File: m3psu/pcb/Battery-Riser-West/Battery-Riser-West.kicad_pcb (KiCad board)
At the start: 2 copper layers, 20 x 67.5 mm, 2 parts, among them J1 WEST TOP, J2 WEST BOT

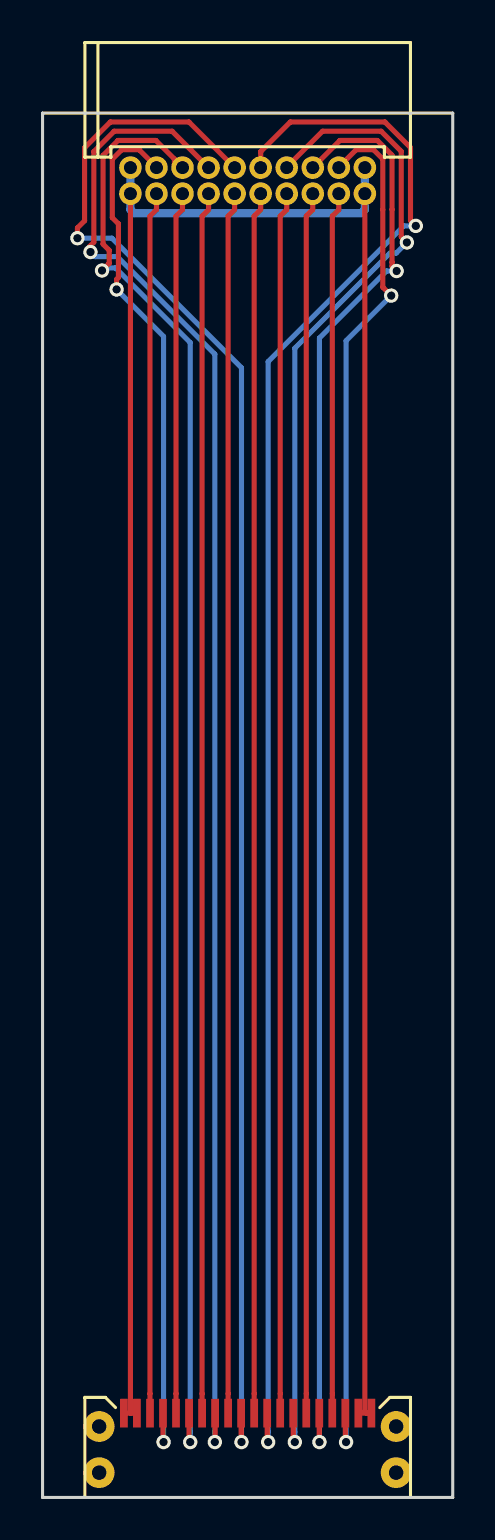
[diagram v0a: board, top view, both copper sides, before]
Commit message: Fix trace widths and spacing on riser boards
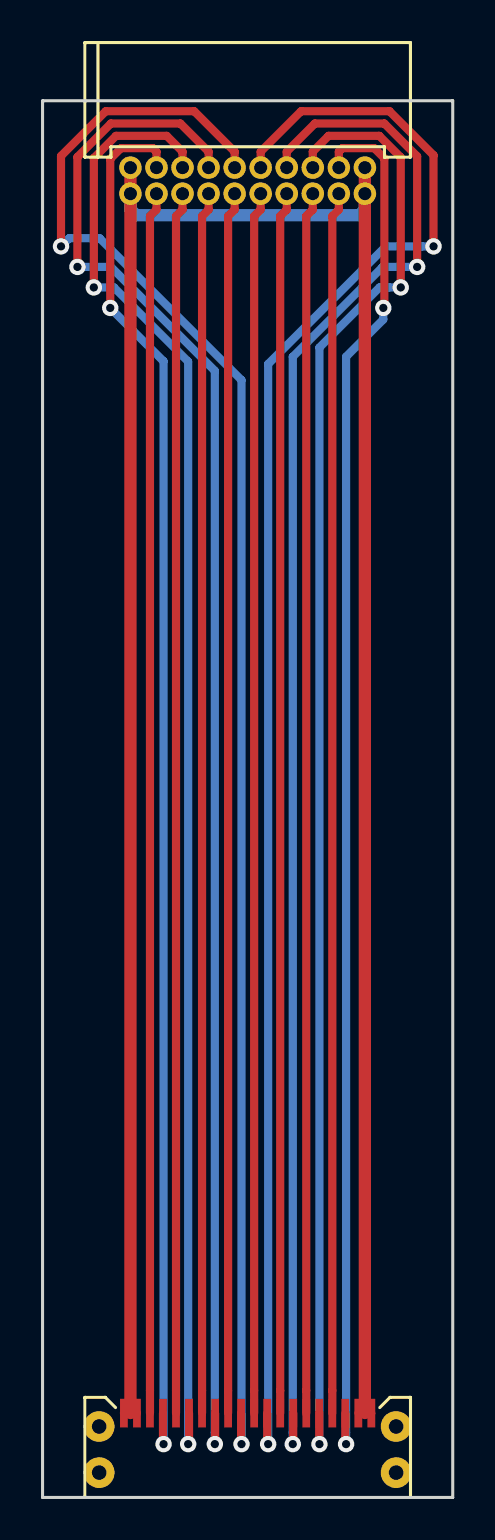
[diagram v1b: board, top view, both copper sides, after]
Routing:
- net /3v3_DL: track 77.7 -> 80.6 mm
- net /3v3_PYRO: track 77.2 -> 80.0 mm
- net /3v3_FC: track 73.7 -> 76.2 mm
- net /3v3_AUX1: track 74.3 -> 76.4 mm
- net /3v3_RADIO: track 70.8 -> 72.3 mm
- net /RSVD3: track 71.7 -> 72.6 mm
- net /RSVD2: track 67.8 -> 68.6 mm
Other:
- board size 20 x 67.5 mm -> 20 x 68.1 mm

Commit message: Widen tracks, add logo, fix DRC errors in West riser.
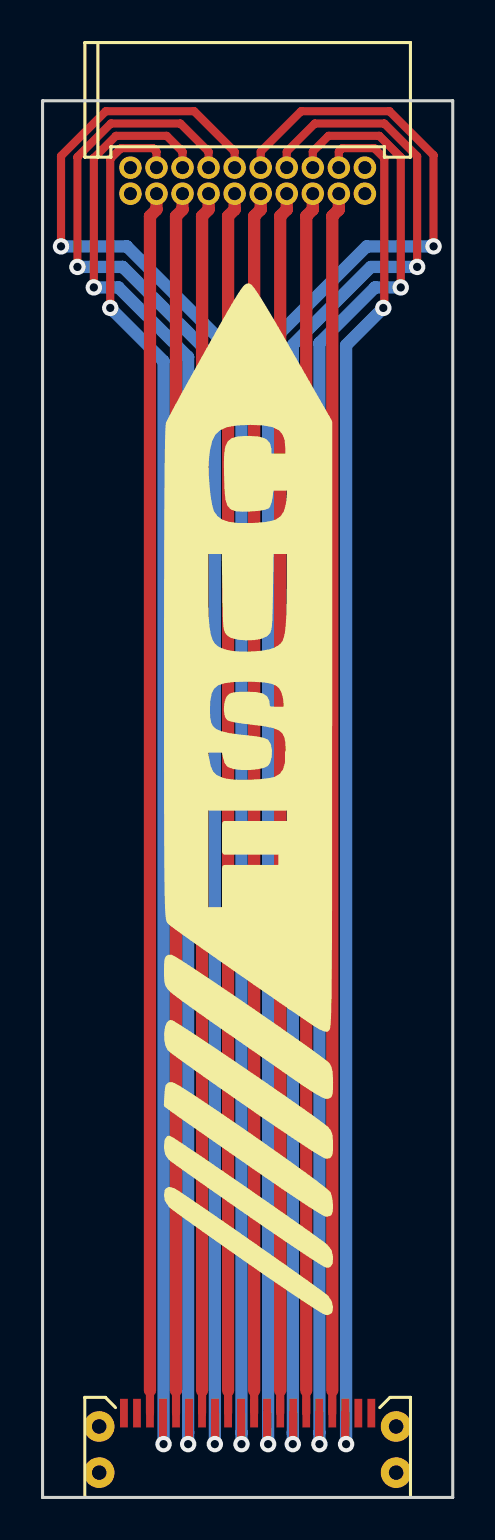
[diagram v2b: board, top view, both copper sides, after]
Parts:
- added G***: LOGO, m3psu:cusf_logo_large, F.Cu at (156.0, 96.0)
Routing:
- net GND: track 135.9 -> 0.00 mm
- net /3v3_PYRO: track 80.0 -> 80.5 mm
- added copper zone on B.Cu, net GND
- added copper zone on F.Cu, net GND
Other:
- rule pad_to_mask_clearance: 0.2 -> 0.15

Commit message: fix riser ground pour, stitching, silk, mask clearance, generate gerbers
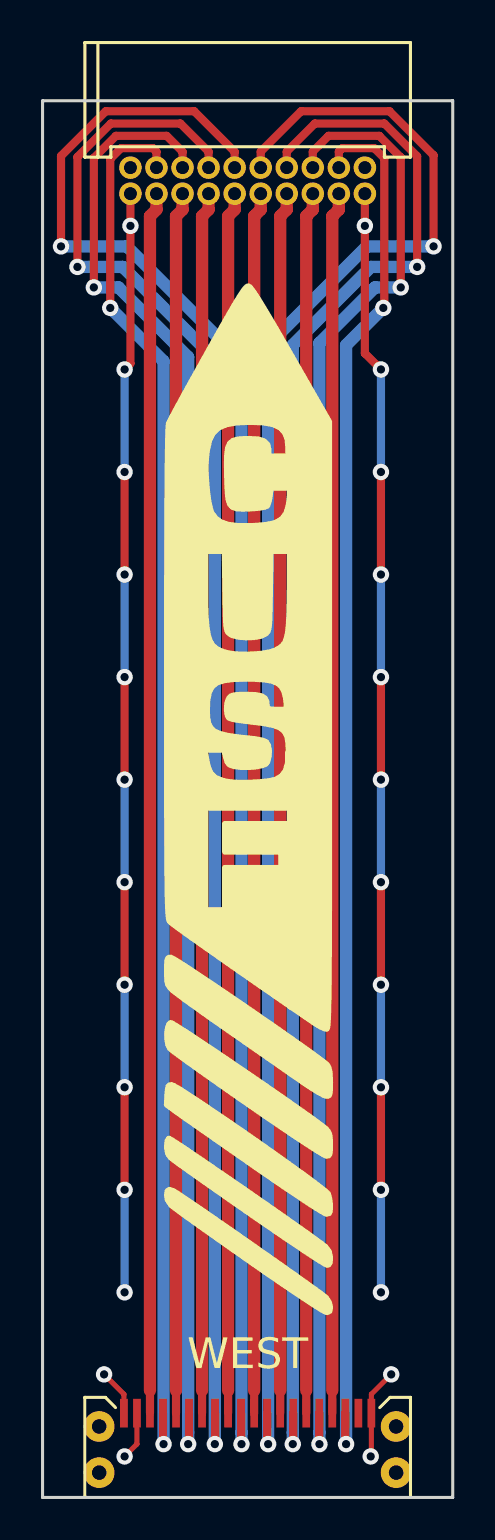
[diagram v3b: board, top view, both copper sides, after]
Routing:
- net GND: track 0.00 -> 119.8 mm, vias 0 -> 26
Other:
- rule pad_to_mask_clearance: 0.15 -> 0
- board text added: "WEST"
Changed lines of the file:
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@@
-(kicad_pcb (version 4) (host pcbnew 4.0.0-rc2-stable)
+(kicad_pcb (version 4) (host pcbnew 4.1.0-alpha+201605071002+6776~44~ubuntu14.04.1-product)
   (general
     (links 23)
     (no_connects 0)
-    (area 145.825 58.644999 166.075001 135.355001)
+    (area 145.924999 58.644999 166.075001 135.355001)
     (thickness 1.6)
-    (drawings 4)
-    (tracks 132)
+    (drawings 5)
+    (tracks 192)
     (zones 0)
     (modules 3)
@@
   (page A4)
   (layers
-    (0 F.Cu signal hide)
-    (31 B.Cu signal hide)
+    (0 F.Cu signal)
+    (31 B.Cu signal)
     (32 B.Adhes user)
     (33 F.Adhes user)
@@
     (user_trace_width 0.8)
     (trace_clearance 0.15)
-    (zone_clearance 0.2)
+    (zone_clearance 0.3)
     (zone_45_only no)
     (trace_min 0.2)
@@
     (pad_size 1.524 1.524)
     (pad_drill 0.762)
-    (pad_to_mask_clearance 0.15)
+    (pad_to_mask_clearance 0)
     (aux_axis_origin 0 0)
     (visible_elements 7FFFFFFF)
     (pcbplotparams
-      (layerselection 0x00030_80000001)
-      (usegerberextensions false)
+      (layerselection 0x010f0_ffffffff)
+      (usegerberextensions true)
       (excludeedgelayer true)
       (linewidth 0.100000)
@@
       (hpglpenspeed 20)
       (hpglpendiameter 15)
-      (hpglpenoverlay 2)
       (psnegative false)
       (psa4output false)
-      (plotreference true)
-      (plotvalue true)
+      (plotreference false)
+      (plotvalue false)
       (plotinvisibletext false)
       (padsonsilk false)
-      (subtractmaskfromsilk false)
+      (subtractmaskfromsilk true)
       (outputformat 1)
       (mirror false)
-      (drillshape 1)
+      (drillshape 0)
       (scaleselection 1)
-      (outputdirectory ""))
+      (outputdirectory gerbers/))
   )
   (net 0 "")
@@
   (module agg:SFM-110-02-L-DH (layer F.Cu)
     (at 156 129.7 180)
-    (fp_text reference J2 (at 9.1 2.6 450) (layer F.Fab)
+    (fp_text reference J2 (at 9.1 2.6 90) (layer F.Fab)
       (effects (font (size 1 1) (thickness 0.15)))
     )
@@
   (module agg:TFML-110-01-L-D-RA (layer F.Cu)
     (at 156 63 180)
-    (fp_text reference J1 (at 9 -2 450) (layer F.Fab)
+    (fp_text reference J1 (at 9 -2 90) (layer F.Fab)
       (effects (font (size 1 1) (thickness 0.15)))
     )
@@
       (xy 3.986213 -3.606549) (xy 3.986213 -3.606549)) (layer F.SilkS) (width 0.27))
   )
+  (gr_text WEST (at 156 123) (layer F.SilkS)
+    (effects (font (size 1.5 1.5) (thickness 0.3)))
+  )
   (gr_line (start 166 130) (end 146 130) (layer Edge.Cuts) (width 0.15))
   (gr_line (start 146 61.9) (end 166 61.9) (layer Edge.Cuts) (width 0.15))
   (gr_line (start 166 61.9) (end 166 130) (layer Edge.Cuts) (width 0.15))
   (gr_line (start 146 130) (end 146 61.9) (layer Edge.Cuts) (width 0.15))
+  (segment (start 161.715 66.429) (end 161.715 68) (width 0.4) (layer F.Cu) (net 1))
+  (segment (start 161.715 68) (end 161.715 74.215) (width 0.4) (layer F.Cu) (net 1))
+  (segment (start 161.715 66.429) (end 161.715 68) (width 0.25) (layer B.Cu) (net 1))
+  (via (at 161.715 68) (size 0.8) (drill 0.4) (layers F.Cu B.Cu) (net 1))
+  (segment (start 150.285 66.429) (end 150.285 68) (width 0.4) (layer F.Cu) (net 1))
+  (segment (start 150.285 68) (end 150.285 74.715) (width 0.4) (layer F.Cu) (net 1))
+  (segment (start 150.285 66.429) (end 150.285 68) (width 0.25) (layer B.Cu) (net 1))
+  (via (at 150.285 68) (size 0.8) (drill 0.4) (layers F.Cu B.Cu) (net 1))
+  (segment (start 162.0325 125.89) (end 162.0325 124.9675) (width 0.25) (layer F.Cu) (net 1))
+  (segment (start 162.0325 124.9675) (end 163 124) (width 0.25) (layer F.Cu) (net 1))
+  (via (at 163 124) (size 0.8) (drill 0.4) (layers F.Cu B.Cu) (net 1))
+  (segment (start 162.0325 125.89) (end 162.0325 127.9675) (width 0.25) (layer F.Cu) (net 1))
+  (segment (start 162.0325 127.9675) (end 162 128) (width 0.25) (layer F.Cu) (net 1))
+  (via (at 162 128) (size 0.8) (drill 0.4) (layers F.Cu B.Cu) (net 1))
+  (segment (start 150.6025 125.89) (end 150.6025 127.3975) (width 0.25) (layer F.Cu) (net 1))
+  (segment (start 150.6025 127.3975) (end 150 128) (width 0.25) (layer F.Cu) (net 1))
+  (via (at 150 128) (size 0.8) (drill 0.4) (layers F.Cu B.Cu) (net 1))
+  (segment (start 149.9675 125.89) (end 149.9675 124.9675) (width 0.25) (layer F.Cu) (net 1))
+  (segment (start 149.9675 124.9675) (end 149 124) (width 0.25) (layer F.Cu) (net 1))
+  (via (at 149 124) (size 0.8) (drill 0.4) (layers F.Cu B.Cu) (net 1))
+  (segment (start 162.5 115) (end 162.5 120) (width 0.4) (layer B.Cu) (net 1))
+  (via (at 162.5 120) (size 0.8) (drill 0.4) (layers F.Cu B.Cu) (net 1))
+  (segment (start 162.5 110) (end 162.5 115) (width 0.4) (layer F.Cu) (net 1))
+  (via (at 162.5 115) (size 0.8) (drill 0.4) (layers F.Cu B.Cu) (net 1))
+  (segment (start 162.5 105) (end 162.5 110) (width 0.4) (layer B.Cu) (net 1))
+  (via (at 162.5 110) (size 0.8) (drill 0.4) (layers F.Cu B.Cu) (net 1))
+  (segment (start 162.5 100) (end 162.5 105) (width 0.4) (layer F.Cu) (net 1))
+  (via (at 162.5 105) (size 0.8) (drill 0.4) (layers F.Cu B.Cu) (net 1))
+  (segment (start 162.5 95) (end 162.5 100) (width 0.4) (layer B.Cu) (net 1))
+  (via (at 162.5 100) (size 0.8) (drill 0.4) (layers F.Cu B.Cu) (net 1))
+  (segment (start 162.5 90) (end 162.5 95) (width 0.4) (layer F.Cu) (net 1))
+  (via (at 162.5 95) (size 0.8) (drill 0.4) (layers F.Cu B.Cu) (net 1))
+  (segment (start 162.5 85) (end 162.5 90) (width 0.4) (layer B.Cu) (net 1))
+  (via (at 162.5 90) (size 0.8) (drill 0.4) (layers F.Cu B.Cu) (net 1))
+  (segment (start 162.5 80) (end 162.5 85) (width 0.4) (layer F.Cu) (net 1))
+  (via (at 162.5 85) (size 0.8) (drill 0.4) (layers F.Cu B.Cu) (net 1))
+  (segment (start 162.5 75) (end 162.5 80) (width 0.4) (layer B.Cu) (net 1))
+  (via (at 162.5 80) (size 0.8) (drill 0.4) (layers F.Cu B.Cu) (net 1))
+  (segment (start 161.715 74.215) (end 162.5 75) (width 0.4) (layer F.Cu) (net 1))
+  (via (at 162.5 75) (size 0.8) (drill 0.4) (layers F.Cu B.Cu) (net 1))
+  (segment (start 150 115) (end 150 120) (width 0.4) (layer B.Cu) (net 1))
+  (via (at 150 120) (size 0.8) (drill 0.4) (layers F.Cu B.Cu) (net 1))
+  (segment (start 150 110) (end 150 115) (width 0.4) (layer F.Cu) (net 1))
+  (via (at 150 115) (size 0.8) (drill 0.4) (layers F.Cu B.Cu) (net 1))
+  (segment (start 150 105) (end 150 110) (width 0.4) (layer B.Cu) (net 1))
+  (via (at 150 110) (size 0.8) (drill 0.4) (layers F.Cu B.Cu) (net 1))
+  (segment (start 150 100) (end 150 105) (width 0.4) (layer F.Cu) (net 1))
+  (via (at 150 105) (size 0.8) (drill 0.4) (layers F.Cu B.Cu) (net 1))
+  (segment (start 150 95) (end 150 100) (width 0.4) (layer B.Cu) (net 1))
+  (via (at 150 100) (size 0.8) (drill 0.4) (layers F.Cu B.Cu) (net 1))
+  (segment (start 150 90) (end 150 95) (width 0.4) (layer F.Cu) (net 1))
+  (via (at 150 95) (size 0.8) (drill 0.4) (layers F.Cu B.Cu) (net 1))
+  (segment (start 150 85) (end 150 90) (width 0.4) (layer B.Cu) (net 1))
+  (via (at 150 90) (size 0.8) (drill 0.4) (layers F.Cu B.Cu) (net 1))
+  (segment (start 150 80) (end 150 85) (width 0.4) (layer F.Cu) (net 1))
+  (via (at 150 85) (size 0.8) (drill 0.4) (layers F.Cu B.Cu) (net 1))
+  (segment (start 150 75) (end 150 80) (width 0.4) (layer B.Cu) (net 1))
+  (via (at 150 80) (size 0.8) (drill 0.4) (layers F.Cu B.Cu) (net 1))
+  (segment (start 150.285 74.715) (end 150 75) (width 0.4) (layer F.Cu) (net 1))
+  (via (at 150 75) (size 0.8) (drill 0.4) (layers F.Cu B.Cu) (net 1))
   (segment (start 160.8 127.4) (end 160.8 73.81501) (width 0.6) (layer B.Cu) (net 2))
   (segment (start 160.8 73.81501) (end 162.61501 72) (width 0.6) (layer B.Cu) (net 2))
@@
   )
   (zone (net 1) (net_name GND) (layer B.Cu) (hatch edge 0.508)
-    (connect_pads (clearance 0.2))
+    (connect_pads (clearance 0.3))
     (min_thickness 0.2)
     (fill yes (arc_segments 16) (thermal_gap 0.15) (thermal_bridge_width 0.3))
